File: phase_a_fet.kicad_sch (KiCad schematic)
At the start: 24 parts, among them Q14 IAUS300N08S5N0, Q15 IAUS300N08S5N0, Q16 IAUS300N08S5N0, Q17 IAUS300N08S5N0, U13 INA241A2

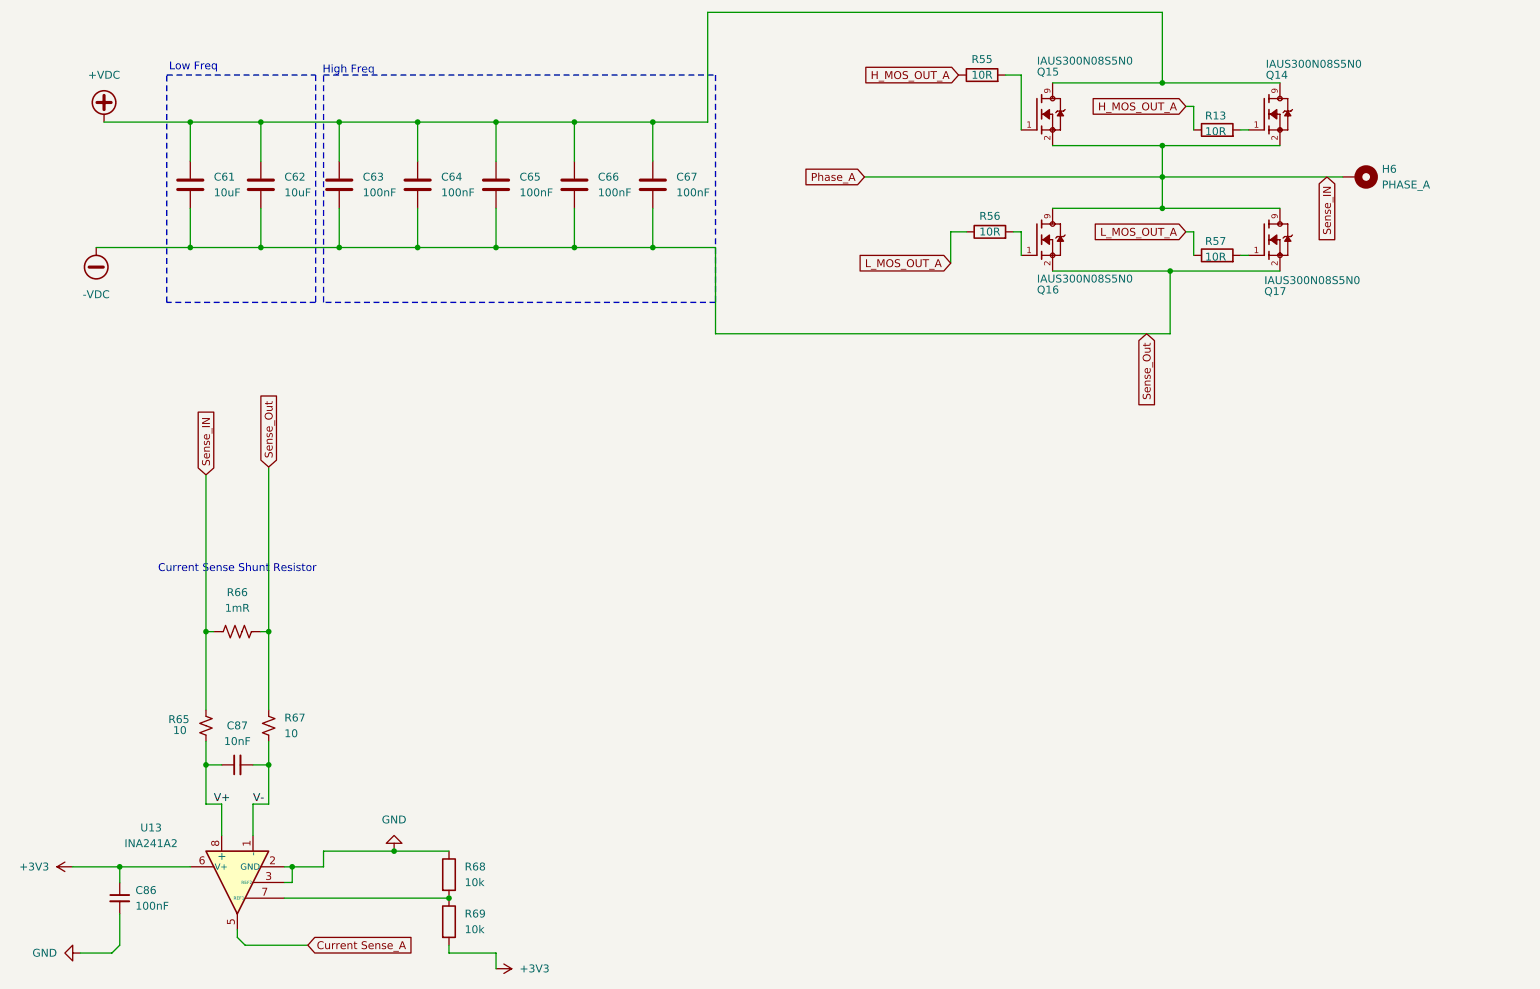
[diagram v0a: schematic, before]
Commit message: update: revised label
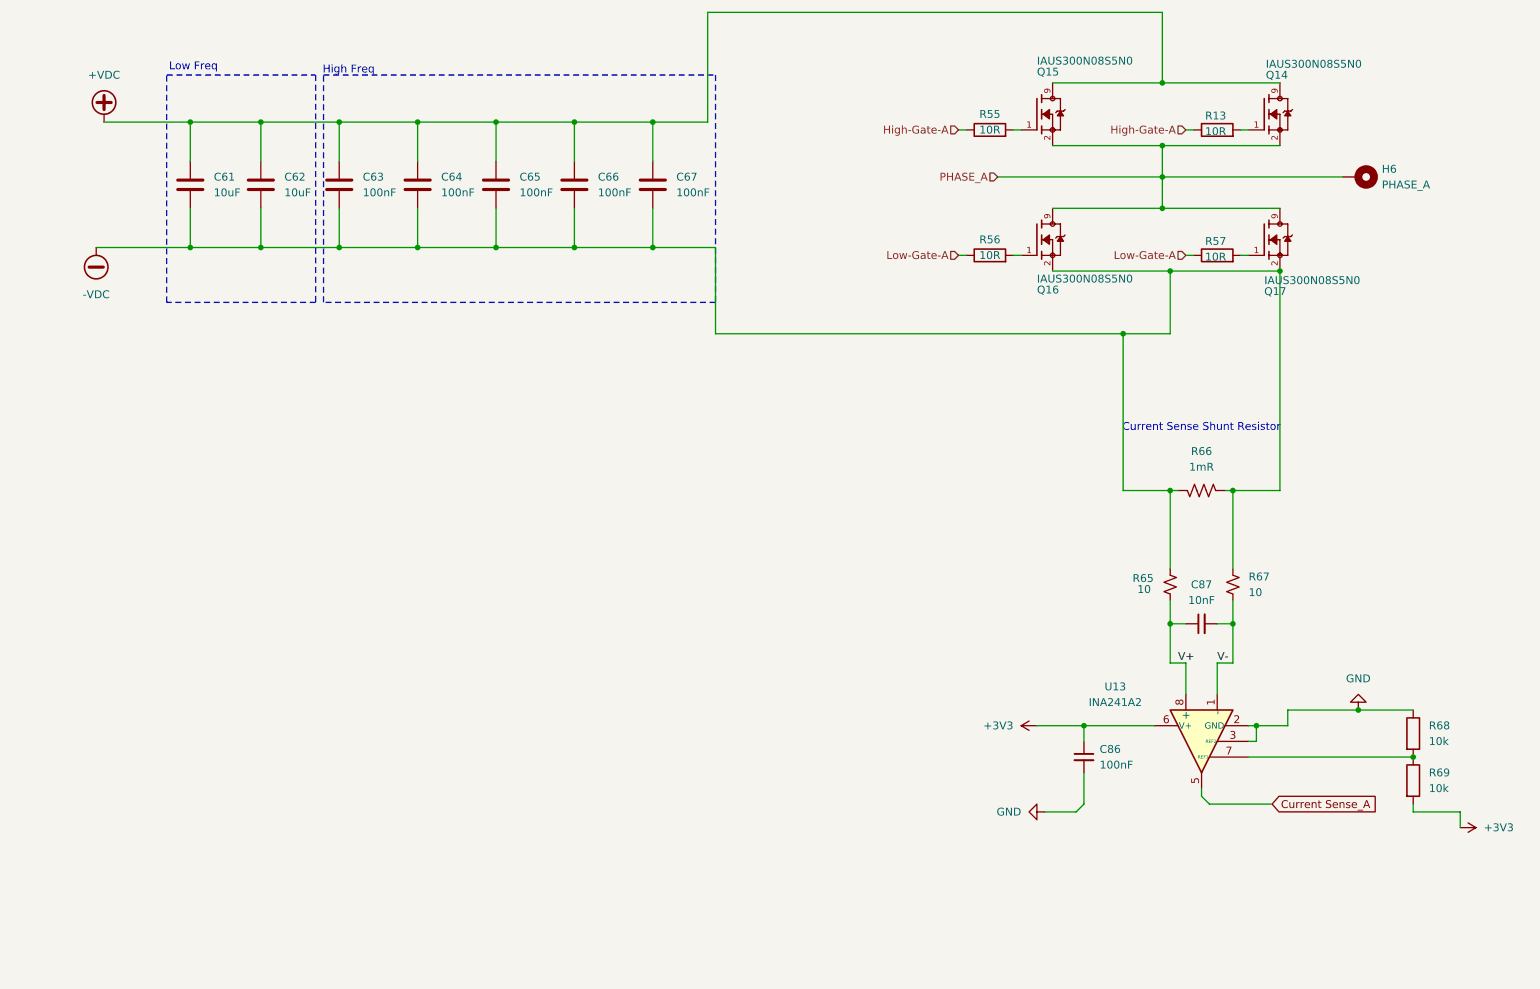
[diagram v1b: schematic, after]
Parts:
- C86, C87: footprint OpenMD:C_0402_1005Metric -> Capacitor_SMD:C_0402_1005Metric_Pad0.74x0.62mm_HandSolder
- R65, R67: footprint OpenMD:R_0402_1005Metric -> Resistor_SMD:R_0402_1005Metric_Pad0.72x0.64mm_HandSolder
- R66: footprint OpenMD:R_2512_6332Metric -> Resistor_SMD:R_2512_6332Metric_Pad1.40x3.35mm_HandSolder
- R68, R69: footprint (none) -> Resistor_SMD:R_1812_4532Metric_Pad1.30x3.40mm_HandSolder
- U13: footprint OpenMD:SOT-23-8 -> Package_TO_SOT_SMD:SOT-23-8_Handsoldering
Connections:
- net -VDC: now also R65.1, R66.1
- net H_MOS_OUT_A renamed High-Gate-A
- net L_MOS_OUT_A renamed Low-Gate-A
- net Phase_A renamed PHASE_A
- net PHASE_A: no longer R65.1, R66.1
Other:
- moved on the sheet: C86, C87, R55, R56, R65, R66, R67, R68, R69, U13

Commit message: LAST I HOPE
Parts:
- added R71: 1mR, Resistor_SMD:R_2512_6332Metric_Pad1.40x3.35mm_HandSolder, symbol OpenMD:R_US
- R68, R69: footprint Resistor_SMD:R_1812_4532Metric_Pad1.30x3.40mm_HandSolder -> Resistor_SMD:R_0603_1608Metric_Pad0.98x0.95mm_HandSolder
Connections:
- net -VDC: now also R71.1, R71.2
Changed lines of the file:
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@@
 	)
 	(junction
+		(at 226.06 106.68)
+		(diameter 0)
+		(color 0 0 0 0)
+	)
+	(junction
 		(at 224.79 45.72)
 		(diameter 0)
@@
 	)
 	(junction
+		(at 236.22 106.68)
+		(diameter 0)
+		(color 0 0 0 0)
+	)
+	(junction
 		(at 91.44 62.23)
 		(diameter 0)
@@
 	(wire
 		(pts
-			(xy 226.06 101.6) (xy 226.06 114.3)
+			(xy 226.06 101.6) (xy 226.06 106.68)
 		)
 		(stroke
@@
 	(wire
 		(pts
+			(xy 226.06 106.68) (xy 227.33 106.68)
+		)
+		(stroke
+			(width 0)
+			(type default)
+		)
+	)
+	(wire
+		(pts
+			(xy 234.95 106.68) (xy 236.22 106.68)
+		)
+		(stroke
+			(width 0)
+			(type default)
+		)
+	)
+	(wire
+		(pts
+			(xy 236.22 106.68) (xy 236.22 114.3)
+		)
+		(stroke
+			(width 0)
+			(type default)
+		)
+	)
+	(wire
+		(pts
 			(xy 233.68 129.54) (xy 233.68 134.62)
 		)
@@
 	(wire
 		(pts
-			(xy 236.22 101.6) (xy 236.22 114.3)
+			(xy 236.22 101.6) (xy 236.22 106.68)
 		)
 		(stroke
@@
 	(wire
 		(pts
+			(xy 226.06 106.68) (xy 226.06 114.3)
+		)
+		(stroke
+			(width 0)
+			(type default)
+		)
+	)
+	(wire
+		(pts
 			(xy 67.31 41.91) (xy 78.74 41.91)
 		)
@@
 			)
 		)
-		(property "Footprint" "Resistor_SMD:R_1812_4532Metric_Pad1.30x3.40mm_HandSolder"
+		(property "Footprint" "Resistor_SMD:R_0603_1608Metric_Pad0.98x0.95mm_HandSolder"
 			(at 263.652 140.97 90)
 			(effects
@@
 			)
 		)
-		(property "Footprint" "Resistor_SMD:R_1812_4532Metric_Pad1.30x3.40mm_HandSolder"
+		(property "Footprint" "Resistor_SMD:R_0603_1608Metric_Pad0.98x0.95mm_HandSolder"
 			(at 263.652 148.59 90)
 			(effects
@@
 					(unit 1)
 				)
+			)
+		)
+	)
+	(symbol
+		(lib_id "OpenMD:R_US")
+		(at 231.14 106.68 90)
+		(unit 1)
+		(exclude_from_sim no)
+		(in_bom yes)
+		(on_board yes)
+		(dnp no)
+		(fields_autoplaced yes)
+		(property "Reference" "R71"
+			(at 231.14 100.33 90)
+			(effects
+				(font
+					(size 1.27 1.27)
+				)
+			)
+		)
+		(property "Value" "1mR"
+			(at 231.14 102.87 90)
+			(effects
+				(font
+					(size 1.27 1.27)
+				)
+			)
+		)
+		(property "Footprint" "Resistor_SMD:R_2512_6332Metric_Pad1.40x3.35mm_HandSolder"
+			(at 231.394 105.664 90)
+			(effects
+				(font
+					(size 1.27 1.27)
+				)
+				(hide yes)
+			)
+		)
+		(property "Datasheet" "~"
+			(at 231.14 106.68 0)
+			(effects
+				(font
+					(size 1.27 1.27)
+				)
+				(hide yes)
+			)
+		)
+		(property "Description" "Resistor, US symbol"
+			(at 231.14 106.68 0)
+			(effects
+				(font
+					(size 1.27 1.27)
+				)
+				(hide yes)
+			)
+		)
+		(property "Rating" "3W"
+			(at 231.14 106.68 0)
+			(effects
+				(font
+					(size 1.27 1.27)
+				)
+				(hide yes)
+			)
+		)
+		(property "Source" "LCSC"
+			(at 231.14 106.68 0)
+			(effects
+				(font
+					(size 1.27 1.27)
+				)
+				(hide yes)
+			)
+		)
+		(property "Manufacturer_Part_Number" "ASR-M-3-0.5F"
+			(at 231.14 106.68 0)
+			(effects
+				(font
+					(size 1.27 1.27)
+				)
+				(hide yes)
+			)
+		)
+		(pin "2"
+		)
+		(pin "1"
+		)
+		(instances
+			(project "Motor_Driver_Shell_Eco"
+				(path "/63ef3b9c-05f1-4b00-812a-fede2372efc7/7c8dbef5-e40c-461c-862c-3f756f947d60/d04a7baa-48a3-44bc-a96a-e075eac02d69"
+					(reference "R71")
+					(unit 1)
+				)

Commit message: rev3
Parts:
- removed H6: PHASE_A, MountingHole:MountingHole_3.7mm_Pad_Via, symbol Mechanical:MountingHole_Pad
- added MP1: Phase_A, WP-BUTR:WP-BUTR_7460307, symbol WP-BUTR:WP-BUTR
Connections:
- net GND is gone; now on net -VDC: C86.2, R68.1, U13.2 (GND), U13.3 (REF2), U13.4 (GND)
- net -VDC: no longer Q16.2, Q16.3, Q16.4, Q16.5, Q16.6, Q16.7, Q16.8, Q17.2, Q17.3, Q17.4, Q17.5, Q17.6, Q17.7, Q17.8, R66.1, R67.1, R71.2
- net PHASE_A: now also MP1.1, MP1.2, MP1.3, MP1.4, MP1.5, MP1.6, MP1.7, MP1.8
- net +3V3 renamed +3V3F
- new net: Q16.2, Q16.3, Q16.4, Q16.5, Q16.6, Q16.7, Q16.8, Q17.2, Q17.3, Q17.4, Q17.5, Q17.6, Q17.7, Q17.8, R66.1, R67.1, R71.2
